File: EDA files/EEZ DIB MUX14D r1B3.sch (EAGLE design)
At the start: 64 parts, among them IC1 STM32F030C6T6, IC2 74HC1G126GW,125, IC3 M24C32-WMN6P, IC4 LP2985-33DBVR, IC5 MCP6001T-I/OT, IC6 LM335AZ, IC7 ULN2803ADWR, IC8 ULN2803ADWR, K1 HE721A0500, K10 HE721A0500, K11 HE721A0500, K12 HE721A0500, K13 HE721A0500, K14 HE721A0500, K15 HE721A0500, K16 HE721A0500, K17 HE721A0500, K2 HE721A0500, K3 HE721A0500, K4 HE721A0500, K5 HE721A0500, K6 HE721A0500, K7 HE721A0500, K8 HE721A0500, K9 HE721A0500, Q1 2N7002, X1 N.C., X2 77317-104-28LF, X3 DS1014-10RF1B, X4 DS1014-10RF1B, X5 691327310016, X6 691327310016

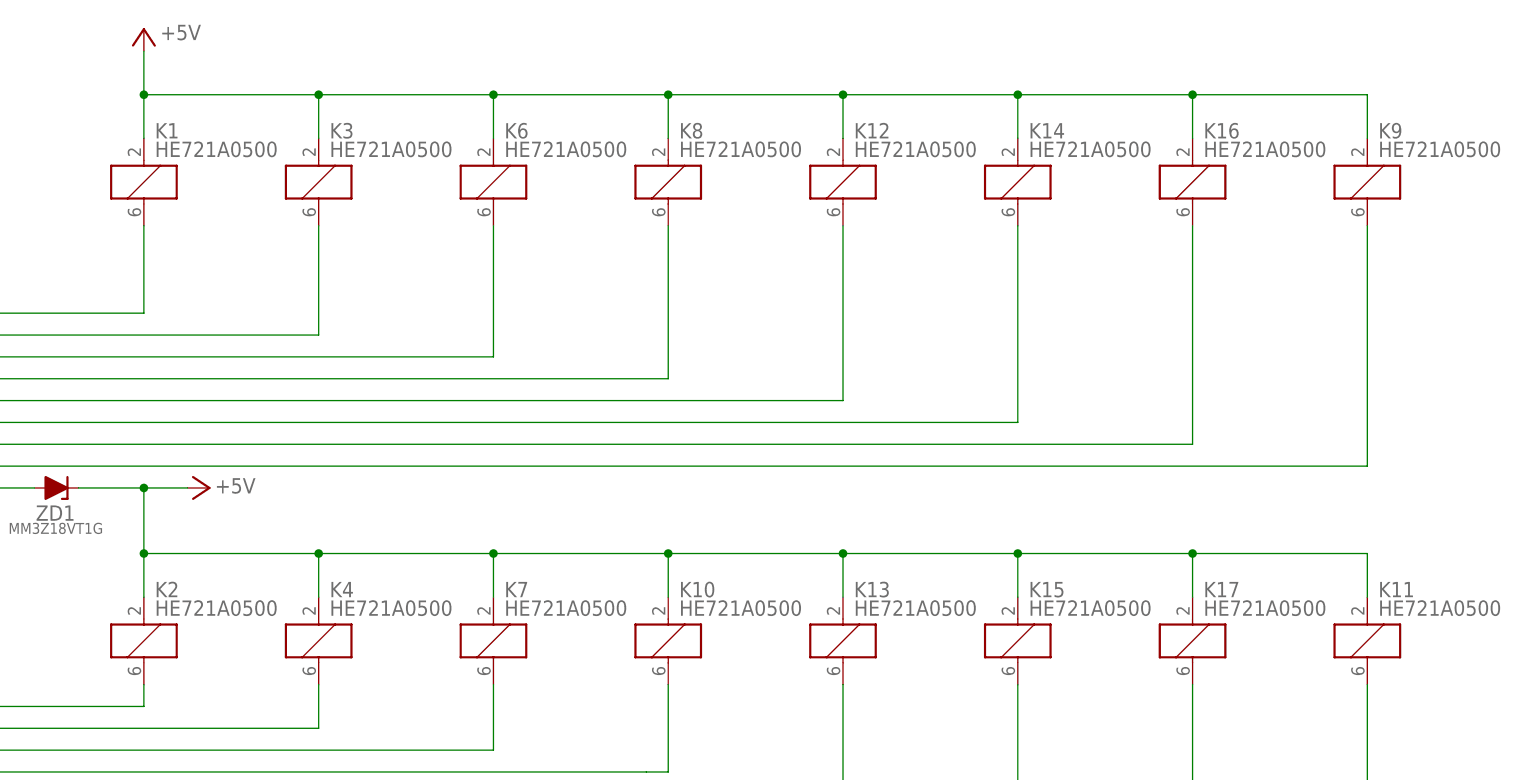
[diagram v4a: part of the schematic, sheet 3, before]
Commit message: Reed relay model correction
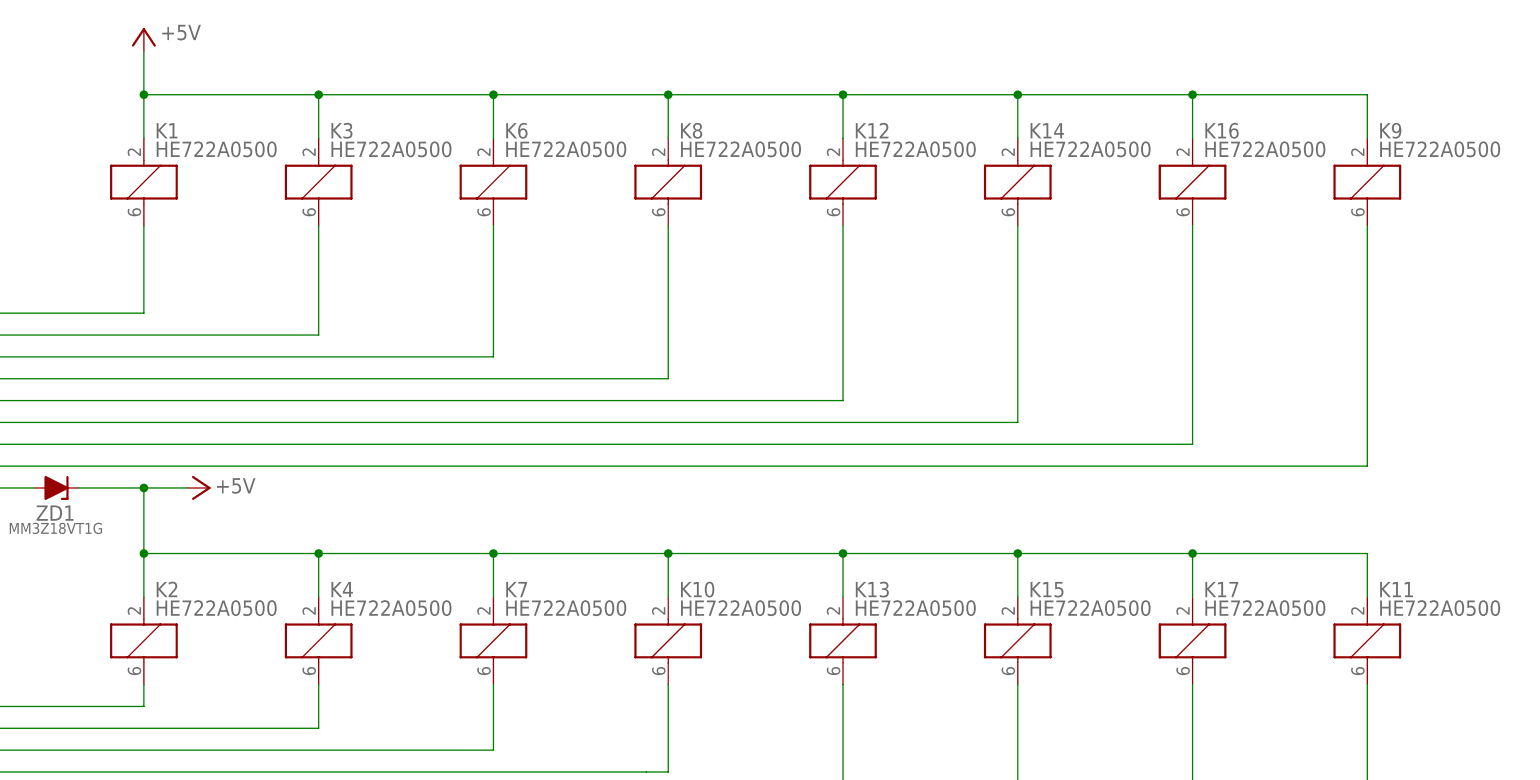
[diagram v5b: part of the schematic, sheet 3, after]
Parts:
- K1, K10, K11, K12, K13, K14, K15, K16, K17, K2, K3, K4, K6, K7, K8, K9: value HE721A0500 -> HE722A0500
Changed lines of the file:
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@@
 <part name="X3" library="EEZ_connectors" deviceset="DS1014-10RF1B" device=""/>
 <part name="X4" library="EEZ_connectors" deviceset="DS1014-10RF1B" device=""/>
-<part name="K1" library="EEZ_switches" deviceset="RR2A" device="" value="HE721A0500"/>
-<part name="K3" library="EEZ_switches" deviceset="RR2A" device="" value="HE721A0500"/>
-<part name="K6" library="EEZ_switches" deviceset="RR2A" device="" value="HE721A0500"/>
-<part name="K8" library="EEZ_switches" deviceset="RR2A" device="" value="HE721A0500"/>
-<part name="K12" library="EEZ_switches" deviceset="RR2A" device="" value="HE721A0500"/>
-<part name="K14" library="EEZ_switches" deviceset="RR2A" device="" value="HE721A0500"/>
-<part name="K16" library="EEZ_switches" deviceset="RR2A" device="" value="HE721A0500"/>
-<part name="K2" library="EEZ_switches" deviceset="RR2A" device="" value="HE721A0500"/>
-<part name="K4" library="EEZ_switches" deviceset="RR2A" device="" value="HE721A0500"/>
-<part name="K7" library="EEZ_switches" deviceset="RR2A" device="" value="HE721A0500"/>
-<part name="K10" library="EEZ_switches" deviceset="RR2A" device="" value="HE721A0500"/>
-<part name="K13" library="EEZ_switches" deviceset="RR2A" device="" value="HE721A0500"/>
+<part name="K1" library="EEZ_switches" deviceset="RR2A" device="" value="HE722A0500"/>
+<part name="K3" library="EEZ_switches" deviceset="RR2A" device="" value="HE722A0500"/>
+<part name="K6" library="EEZ_switches" deviceset="RR2A" device="" value="HE722A0500"/>
+<part name="K8" library="EEZ_switches" deviceset="RR2A" device="" value="HE722A0500"/>
+<part name="K12" library="EEZ_switches" deviceset="RR2A" device="" value="HE722A0500"/>
+<part name="K14" library="EEZ_switches" deviceset="RR2A" device="" value="HE722A0500"/>
+<part name="K16" library="EEZ_switches" deviceset="RR2A" device="" value="HE722A0500"/>
+<part name="K2" library="EEZ_switches" deviceset="RR2A" device="" value="HE722A0500"/>
+<part name="K4" library="EEZ_switches" deviceset="RR2A" device="" value="HE722A0500"/>
+<part name="K7" library="EEZ_switches" deviceset="RR2A" device="" value="HE722A0500"/>
+<part name="K10" library="EEZ_switches" deviceset="RR2A" device="" value="HE722A0500"/>
+<part name="K13" library="EEZ_switches" deviceset="RR2A" device="" value="HE722A0500"/>
 <part name="ZD1" library="EEZ_Lib1" deviceset="ZENER-DIODE" device="SOD323R" value="MM3Z18VT1G"/>
 <part name="ZD2" library="EEZ_Lib1" deviceset="ZENER-DIODE" device="SOD323R" value="MM3Z18VT1G"/>
@@
 <part name="P+6" library="supply1" deviceset="+5V" device=""/>
 <part name="P+5" library="supply1" deviceset="+5V" device=""/>
-<part name="K15" library="EEZ_switches" deviceset="RR2A" device="" value="HE721A0500"/>
-<part name="K17" library="EEZ_switches" deviceset="RR2A" device="" value="HE721A0500"/>
-<part name="K9" library="EEZ_switches" deviceset="RR2A" device="" value="HE721A0500"/>
-<part name="K11" library="EEZ_switches" deviceset="RR2A" device="" value="HE721A0500"/>
+<part name="K15" library="EEZ_switches" deviceset="RR2A" device="" value="HE722A0500"/>
+<part name="K17" library="EEZ_switches" deviceset="RR2A" device="" value="HE722A0500"/>
+<part name="K9" library="EEZ_switches" deviceset="RR2A" device="" value="HE722A0500"/>
+<part name="K11" library="EEZ_switches" deviceset="RR2A" device="" value="HE722A0500"/>
 <part name="K5" library="EEZ_switches" deviceset="RR2A" device="" value="HE721A0500"/>
 <part name="P+4" library="supply1" deviceset="+5V" device=""/>
